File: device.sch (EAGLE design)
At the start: 33 parts, among them J1 10103594-0001LF, P1 ST9S008V4AR1500, P2 S2B-PH-SM4-TB(LF)(SN), Q1 FDN340P, U1 RPI_COMPUTE, U2 LMR10510YMFE/NOPB, U3 LMR10510YMFE/NOPB, U4 MCP73832T-2ACI/OT

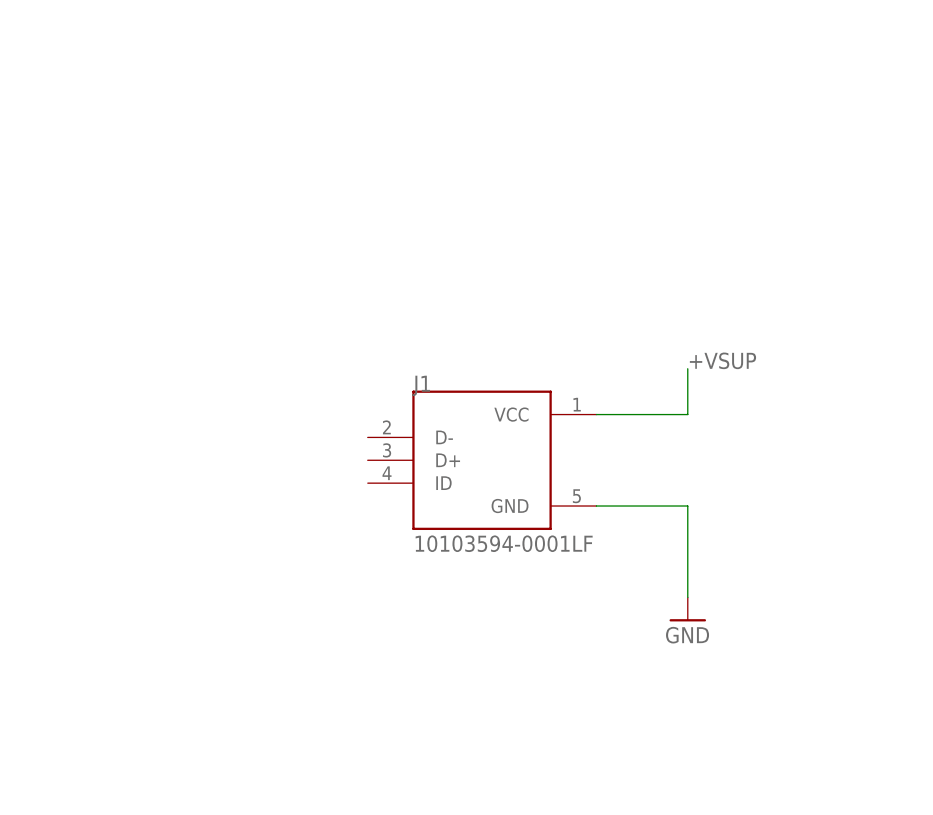
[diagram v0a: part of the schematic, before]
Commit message: Add usb-c
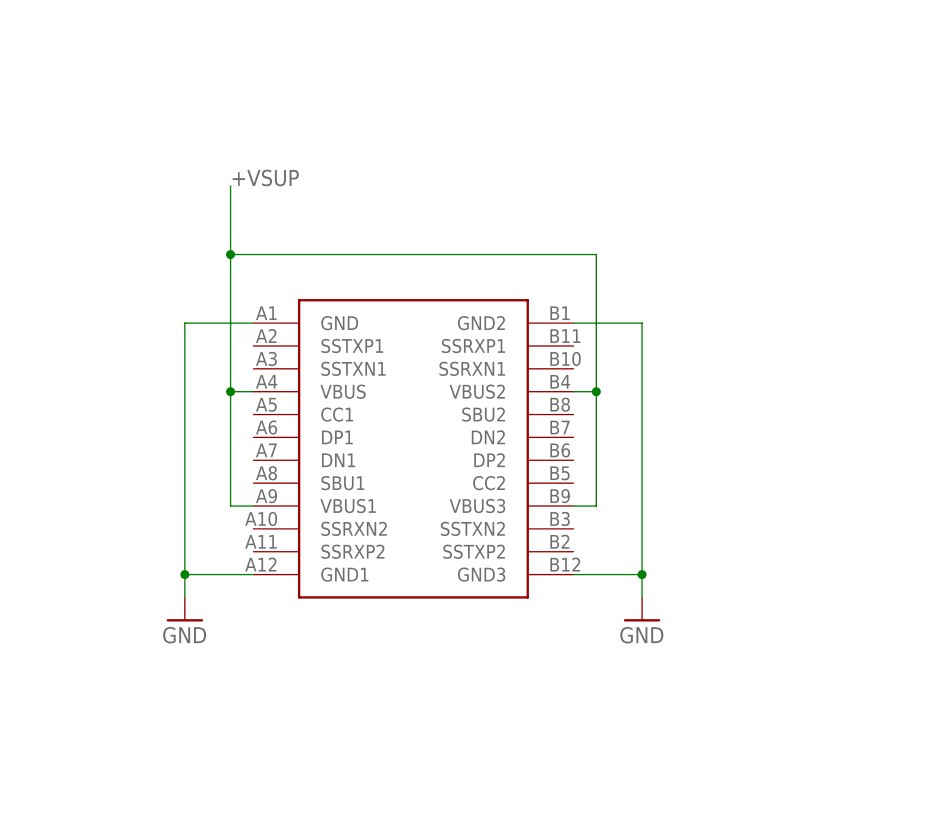
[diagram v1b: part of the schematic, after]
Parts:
- removed J1: 10103594-0001LF, Common-Parts-Library-Eagle:10103594-0001LF
- added SUPPLY: (no value), Wurth_Elektronik_Electromechanic_Input-Output_Connectors_rev17b:632723100011
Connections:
- net +VSUP: now also SUPPLYG$1.VBUS, SUPPLYG$1.VBUS1, SUPPLYG$1.VBUS2, SUPPLYG$1.VBUS3; no longer J1.VCC
- net GND: now also SUPPLYG$1.GND, SUPPLYG$1.GND1, SUPPLYG$1.GND2, SUPPLYG$1.GND3; no longer J1.GND
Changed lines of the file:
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@@
 <layer number="112" name="tSilk" color="7" fill="1" visible="no" active="yes"/>
 <layer number="113" name="ReferenceLS" color="7" fill="1" visible="no" active="no"/>
+<layer number="114" name="FRNTMAAT1" color="7" fill="1" visible="no" active="no"/>
+<layer number="115" name="FRNTMAAT2" color="7" fill="1" visible="no" active="no"/>
 <layer number="116" name="Patch_BOT" color="9" fill="4" visible="no" active="yes"/>
+<layer number="117" name="BACKMAAT1" color="7" fill="1" visible="no" active="no"/>
 <layer number="118" name="Rect_Pads" color="7" fill="1" visible="no" active="no"/>
+<layer number="119" name="KAP_TEKEN" color="7" fill="1" visible="no" active="no"/>
+<layer number="120" name="KAP_MAAT1" color="7" fill="1" visible="no" active="no"/>
 <layer number="121" name="_tsilk" color="7" fill="1" visible="no" active="yes"/>
 <layer number="122" name="_bsilk" color="7" fill="1" visible="no" active="yes"/>
@@
 <layer number="128" name="_bValues" color="7" fill="1" visible="no" active="yes"/>
 <layer number="129" name="Mask" color="7" fill="1" visible="yes" active="yes"/>
+<layer number="130" name="SMDSTROOK" color="7" fill="1" visible="no" active="no"/>
 <layer number="131" name="tAdjust" color="7" fill="1" visible="no" active="yes"/>
 <layer number="132" name="bAdjust" color="7" fill="1" visible="no" active="yes"/>
+<layer number="133" name="bottom_silk" color="7" fill="1" visible="no" active="no"/>
+<layer number="134" name="silk_top" color="7" fill="1" visible="no" active="no"/>
+<layer number="135" name="silk_bottom" color="7" fill="1" visible="no" active="no"/>
+<layer number="136" name="silktop" color="7" fill="1" visible="yes" active="yes"/>
+<layer number="137" name="silkbottom" color="7" fill="1" visible="yes" active="yes"/>
 <layer number="144" name="Drill_legend" color="7" fill="1" visible="no" active="yes"/>
+<layer number="145" name="DrillLegend_01-16" color="7" fill="1" visible="yes" active="yes"/>
+<layer number="146" name="DrillLegend_01-20" color="7" fill="1" visible="yes" active="yes"/>
 <layer number="150" name="Notes" color="7" fill="1" visible="no" active="yes"/>
 <layer number="151" name="HeatSink" color="7" fill="1" visible="no" active="yes"/>
@@
 <layer number="154" name="FabDoc2" color="2" fill="1" visible="no" active="no"/>
 <layer number="155" name="FabDoc3" color="7" fill="15" visible="no" active="no"/>
+<layer number="166" name="AntennaArea" color="7" fill="1" visible="yes" active="yes"/>
+<layer number="168" name="4mmHeightArea" color="7" fill="1" visible="yes" active="yes"/>
 <layer number="199" name="Contour" color="7" fill="1" visible="no" active="yes"/>
 <layer number="200" name="200bmp" color="1" fill="10" visible="yes" active="yes"/>
@@
 <part name="P2" library="Common-Parts-Library-Eagle" deviceset="S2B-PH-SM4-TB(LF)(SN)" device=""/>
 <part name="GND10" library="supply1" library_urn="urn:adsk.eagle:library:371" deviceset="GND" device=""/>
-<part name="J1" library="Common-Parts-Library-Eagle" deviceset="10103594-0001LF" device=""/>
-<part name="GND11" library="supply1" library_urn="urn:adsk.eagle:library:371" deviceset="GND" device=""/>
 <part name="R14" library="resistor" library_urn="urn:adsk.eagle:library:348" deviceset="R-EU_" device="R0603" value="470"/>
 <part name="GND12" library="supply1" library_urn="urn:adsk.eagle:library:371" deviceset="GND" device=""/>
 <part name="POWER" library="led" library_urn="urn:adsk.eagle:library:259" deviceset="LED" device="CHIP-LED0603"/>
+<part name="SUPPLY" library="Wurth_Elektronik_Electromechanic_Input-Output_Connectors_rev17b" library_urn="urn:adsk.eagle:library:449" deviceset="632723100011" device=""/>
+<part name="GND11" library="supply1" library_urn="urn:adsk.eagle:library:371" deviceset="GND" device=""/>
+<part name="GND13" library="supply1" library_urn="urn:adsk.eagle:library:371" deviceset="GND" device=""/>
 </parts>
 <sheets>
@@
 <instance part="P2" gate="G$1" x="358.14" y="520.7"/>
 <instance part="GND10" gate="1" x="342.9" y="513.08"/>
-<instance part="J1" gate="G$1" x="294.64" y="383.54"/>
-<instance part="GND11" gate="1" x="317.5" y="365.76"/>
 <instance part="R14" gate="G$1" x="292.1" y="482.6" rot="R90"/>
 <instance part="GND12" gate="1" x="320.04" y="469.9"/>
 <instance part="POWER" gate="G$1" x="304.8" y="472.44" rot="R90"/>
+<instance part="SUPPLY" gate="G$1" x="287.02" y="383.54"/>
+<instance part="GND11" gate="1" x="312.42" y="365.76"/>
+<instance part="GND13" gate="1" x="261.62" y="365.76"/>
 </instances>
 <busses>
@@
 </segment>
 <segment>
-<pinref part="J1" gate="G$1" pin="GND"/>
-<pinref part="GND11" gate="1" pin="GND"/>
-<wire x1="307.34" y1="378.46" x2="317.5" y2="378.46" width="0.1524" layer="91"/>
-<wire x1="317.5" y1="378.46" x2="317.5" y2="368.3" width="0.1524" layer="91"/>
-</segment>
-<segment>
 <pinref part="POWER" gate="G$1" pin="C"/>
 <pinref part="GND12" gate="1" pin="GND"/>
 <wire x1="309.88" y1="472.44" x2="320.04" y2="472.44" width="0.1524" layer="91"/>
+</segment>
+<segment>
+<pinref part="GND13" gate="1" pin="GND"/>
+<wire x1="261.62" y1="368.3" x2="261.62" y2="370.84" width="0.1524" layer="91"/>
+<pinref part="SUPPLY" gate="G$1" pin="GND1"/>
+<wire x1="261.62" y1="370.84" x2="269.24" y2="370.84" width="0.1524" layer="91"/>
+<pinref part="SUPPLY" gate="G$1" pin="GND"/>
+<wire x1="269.24" y1="398.78" x2="261.62" y2="398.78" width="0.1524" layer="91"/>
+<wire x1="261.62" y1="398.78" x2="261.62" y2="370.84" width="0.1524" layer="91"/>
+<junction x="261.62" y="370.84"/>
+</segment>
+<segment>
+<pinref part="SUPPLY" gate="G$1" pin="GND3"/>
+<pinref part="GND11" gate="1" pin="GND"/>
+<wire x1="304.8" y1="370.84" x2="312.42" y2="370.84" width="0.1524" layer="91"/>
+<wire x1="312.42" y1="370.84" x2="312.42" y2="368.3" width="0.1524" layer="91"/>
+<pinref part="SUPPLY" gate="G$1" pin="GND2"/>
+<wire x1="304.8" y1="398.78" x2="312.42" y2="398.78" width="0.1524" layer="91"/>
+<wire x1="312.42" y1="398.78" x2="312.42" y2="370.84" width="0.1524" layer="91"/>
+<junction x="312.42" y="370.84"/>
 </segment>
 </net>
@@
 </segment>
 <segment>
-<pinref part="J1" gate="G$1" pin="VCC"/>
-<wire x1="307.34" y1="388.62" x2="317.5" y2="388.62" width="0.1524" layer="91"/>
-<wire x1="317.5" y1="388.62" x2="317.5" y2="393.7" width="0.1524" layer="91"/>
-<label x="317.5" y="393.7" size="1.778" layer="95"/>
-</segment>
-</net>
+<pinref part="SUPPLY" gate="G$1" pin="VBUS"/>
+<wire x1="269.24" y1="391.16" x2="266.7" y2="391.16" width="0.1524" layer="91"/>
+<wire x1="266.7" y1="391.16" x2="266.7" y2="406.4" width="0.1524" layer="91"/>
+<pinref part="SUPPLY" gate="G$1" pin="VBUS1"/>
+<wire x1="266.7" y1="406.4" x2="266.7" y2="414.02" width="0.1524" layer="91"/>
+<wire x1="269.24" y1="378.46" x2="266.7" y2="378.46" width="0.1524" layer="91"/>
+<wire x1="266.7" y1="378.46" x2="266.7" y2="391.16" width="0.1524" layer="91"/>
+<junction x="266.7" y="391.16"/>
+<pinref part="SUPPLY" gate="G$1" pin="VBUS3"/>
+<wire x1="304.8" y1="378.46" x2="307.34" y2="378.46" width="0.1524" layer="91"/>
+<wire x1="307.34" y1="378.46" x2="307.34" y2="391.16" width="0.1524" layer="91"/>
+<wire x1="307.34" y1="391.16" x2="307.34" y2="406.4" width="0.1524" layer="91"/>
+<wire x1="307.34" y1="406.4" x2="266.7" y2="406.4" width="0.1524" layer="91"/>
+<junction x="266.7" y="406.4"/>
+<pinref part="SUPPLY" gate="G$1" pin="VBUS2"/>
+<wire x1="304.8" y1="391.16" x2="307.34" y2="391.16" width="0.1524" layer="91"/>
+<junction x="307.34" y="391.16"/>
+<label x="266.7" y="414.02" size="1.778" layer="95"/>
+</segment>
+</net>

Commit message: Rename to J1
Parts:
- renumbered SUPPLY to J1
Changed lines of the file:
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@@
 <part name="GND12" library="supply1" library_urn="urn:adsk.eagle:library:371" deviceset="GND" device=""/>
 <part name="POWER" library="led" library_urn="urn:adsk.eagle:library:259" deviceset="LED" device="CHIP-LED0603"/>
-<part name="SUPPLY" library="Wurth_Elektronik_Electromechanic_Input-Output_Connectors_rev17b" library_urn="urn:adsk.eagle:library:449" deviceset="632723100011" device=""/>
+<part name="J1" library="Wurth_Elektronik_Electromechanic_Input-Output_Connectors_rev17b" library_urn="urn:adsk.eagle:library:449" deviceset="632723100011" device=""/>
 <part name="GND11" library="supply1" library_urn="urn:adsk.eagle:library:371" deviceset="GND" device=""/>
 <part name="GND13" library="supply1" library_urn="urn:adsk.eagle:library:371" deviceset="GND" device=""/>
@@
 <instance part="GND12" gate="1" x="320.04" y="469.9"/>
 <instance part="POWER" gate="G$1" x="304.8" y="472.44" rot="R90"/>
-<instance part="SUPPLY" gate="G$1" x="287.02" y="383.54"/>
+<instance part="J1" gate="G$1" x="287.02" y="383.54"/>
 <instance part="GND11" gate="1" x="312.42" y="365.76"/>
 <instance part="GND13" gate="1" x="261.62" y="365.76"/>
@@
 <pinref part="GND13" gate="1" pin="GND"/>
 <wire x1="261.62" y1="368.3" x2="261.62" y2="370.84" width="0.1524" layer="91"/>
-<pinref part="SUPPLY" gate="G$1" pin="GND1"/>
+<pinref part="J1" gate="G$1" pin="GND1"/>
 <wire x1="261.62" y1="370.84" x2="269.24" y2="370.84" width="0.1524" layer="91"/>
-<pinref part="SUPPLY" gate="G$1" pin="GND"/>
+<pinref part="J1" gate="G$1" pin="GND"/>
 <wire x1="269.24" y1="398.78" x2="261.62" y2="398.78" width="0.1524" layer="91"/>
 <wire x1="261.62" y1="398.78" x2="261.62" y2="370.84" width="0.1524" layer="91"/>
@@
 </segment>
 <segment>
-<pinref part="SUPPLY" gate="G$1" pin="GND3"/>
+<pinref part="J1" gate="G$1" pin="GND3"/>
 <pinref part="GND11" gate="1" pin="GND"/>
 <wire x1="304.8" y1="370.84" x2="312.42" y2="370.84" width="0.1524" layer="91"/>
 <wire x1="312.42" y1="370.84" x2="312.42" y2="368.3" width="0.1524" layer="91"/>
-<pinref part="SUPPLY" gate="G$1" pin="GND2"/>
+<pinref part="J1" gate="G$1" pin="GND2"/>
 <wire x1="304.8" y1="398.78" x2="312.42" y2="398.78" width="0.1524" layer="91"/>
 <wire x1="312.42" y1="398.78" x2="312.42" y2="370.84" width="0.1524" layer="91"/>
@@
 </segment>
 <segment>
-<pinref part="SUPPLY" gate="G$1" pin="VBUS"/>
+<pinref part="J1" gate="G$1" pin="VBUS"/>
 <wire x1="269.24" y1="391.16" x2="266.7" y2="391.16" width="0.1524" layer="91"/>
 <wire x1="266.7" y1="391.16" x2="266.7" y2="406.4" width="0.1524" layer="91"/>
-<pinref part="SUPPLY" gate="G$1" pin="VBUS1"/>
+<pinref part="J1" gate="G$1" pin="VBUS1"/>
 <wire x1="266.7" y1="406.4" x2="266.7" y2="414.02" width="0.1524" layer="91"/>
 <wire x1="269.24" y1="378.46" x2="266.7" y2="378.46" width="0.1524" layer="91"/>
 <wire x1="266.7" y1="378.46" x2="266.7" y2="391.16" width="0.1524" layer="91"/>
 <junction x="266.7" y="391.16"/>
-<pinref part="SUPPLY" gate="G$1" pin="VBUS3"/>
+<pinref part="J1" gate="G$1" pin="VBUS3"/>
 <wire x1="304.8" y1="378.46" x2="307.34" y2="378.46" width="0.1524" layer="91"/>
 <wire x1="307.34" y1="378.46" x2="307.34" y2="391.16" width="0.1524" layer="91"/>
@@
 <wire x1="307.34" y1="406.4" x2="266.7" y2="406.4" width="0.1524" layer="91"/>
 <junction x="266.7" y="406.4"/>
-<pinref part="SUPPLY" gate="G$1" pin="VBUS2"/>
+<pinref part="J1" gate="G$1" pin="VBUS2"/>
 <wire x1="304.8" y1="391.16" x2="307.34" y2="391.16" width="0.1524" layer="91"/>
 <junction x="307.34" y="391.16"/>
